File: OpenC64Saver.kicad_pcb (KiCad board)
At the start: 2 copper layers, 21 x 46 mm, 17 parts, among them J1 Power I/O, Q1 PN2222A, Q2 PN2222A

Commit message: Remove R2 and reorient trimmer (which is now R2)
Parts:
- removed the R2 at (138.4, 114.6)
- R1: value 2.2k -> 820
- R2: renamed from R7; footprint pth_resistors:trimmer_vishay_64w -> C64Saver:trimmer_vishay_64w
- X1: renamed from G***; value LOGO -> OSHW_LOGO
- X2: renamed from REF**; value 1pin -> SCREW_HOLE
- turned R2 to 0 degrees
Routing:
- net Net-(Q1-Pad2): track 26.0 -> 22.9 mm

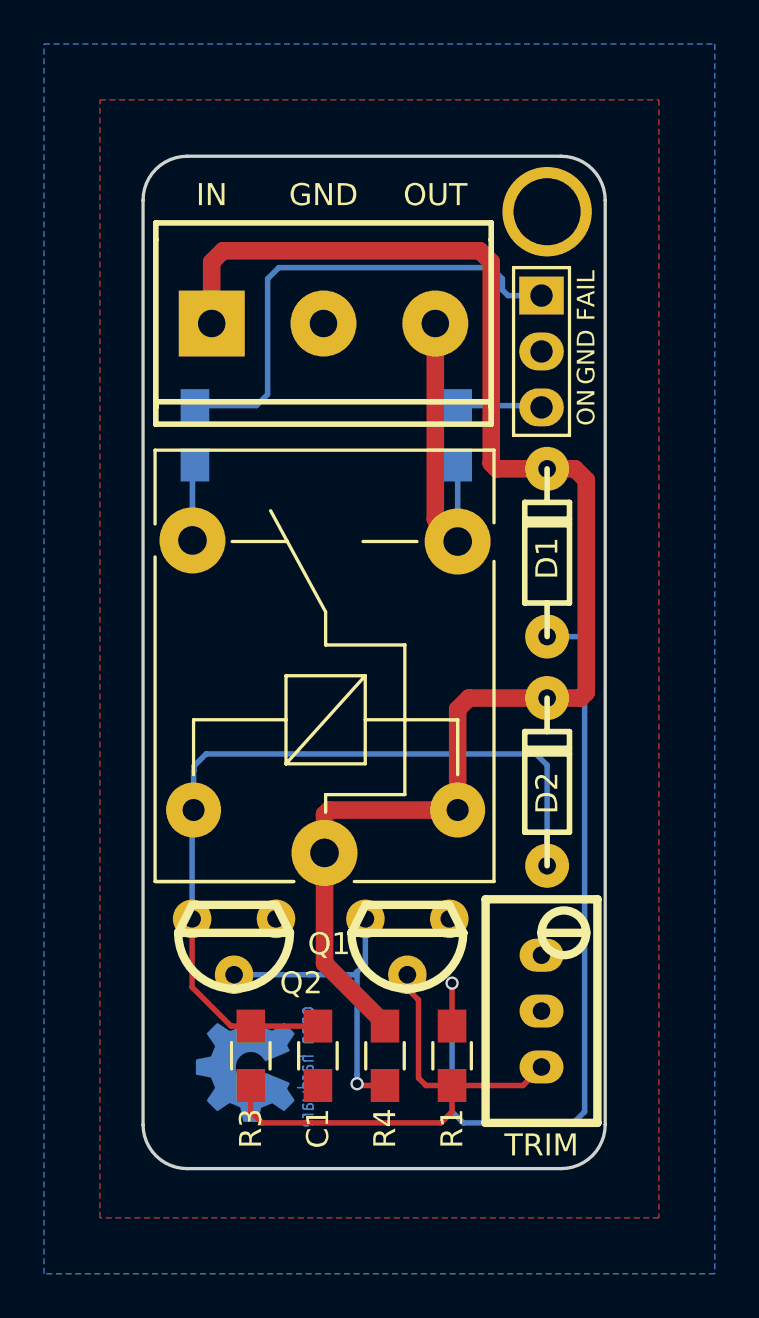
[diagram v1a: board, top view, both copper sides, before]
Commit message: Fit a 2nd screw hole
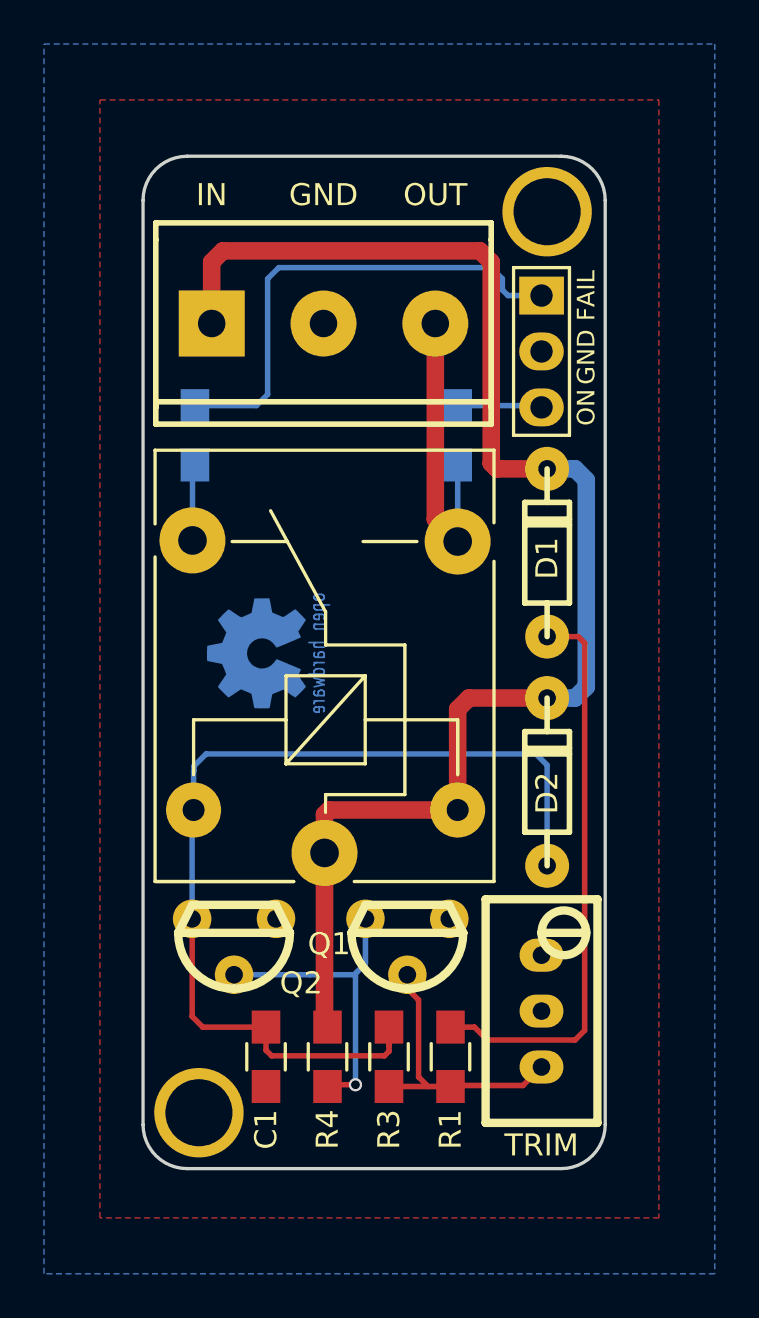
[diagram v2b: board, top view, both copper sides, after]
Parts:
- added X3: SCREW_HOLE, Connectors:1pin, F.Cu at (139.1, 117.1)
- moved X1 18.8 mm to (141.7, 96.3)
- moved R3 6.28 mm to (147.8, 114.6)
- moved R4 2.61 mm to (145.0, 114.6)
- moved C1 2.36 mm to (142.2, 114.6)
- moved R1 0.09 mm to (150.6, 114.6)
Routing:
- net Net-(D1-Pad2): track 37.4 -> 26.0 mm, vias 1 -> 0
- net Net-(Q1-Pad2): track 22.9 -> 12.7 mm
- net Net-(C1-Pad1): track 37.6 -> 44.1 mm
- net VCC: track 67.0 -> 65.8 mm
